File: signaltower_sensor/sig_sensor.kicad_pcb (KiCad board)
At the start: 2 copper layers, 44.6 x 39.3 mm, 6 parts, among them J1 5051100892_FFC-FPC_in, J2 5051100892_FFC-FPC_out, U1 BH1620FVC

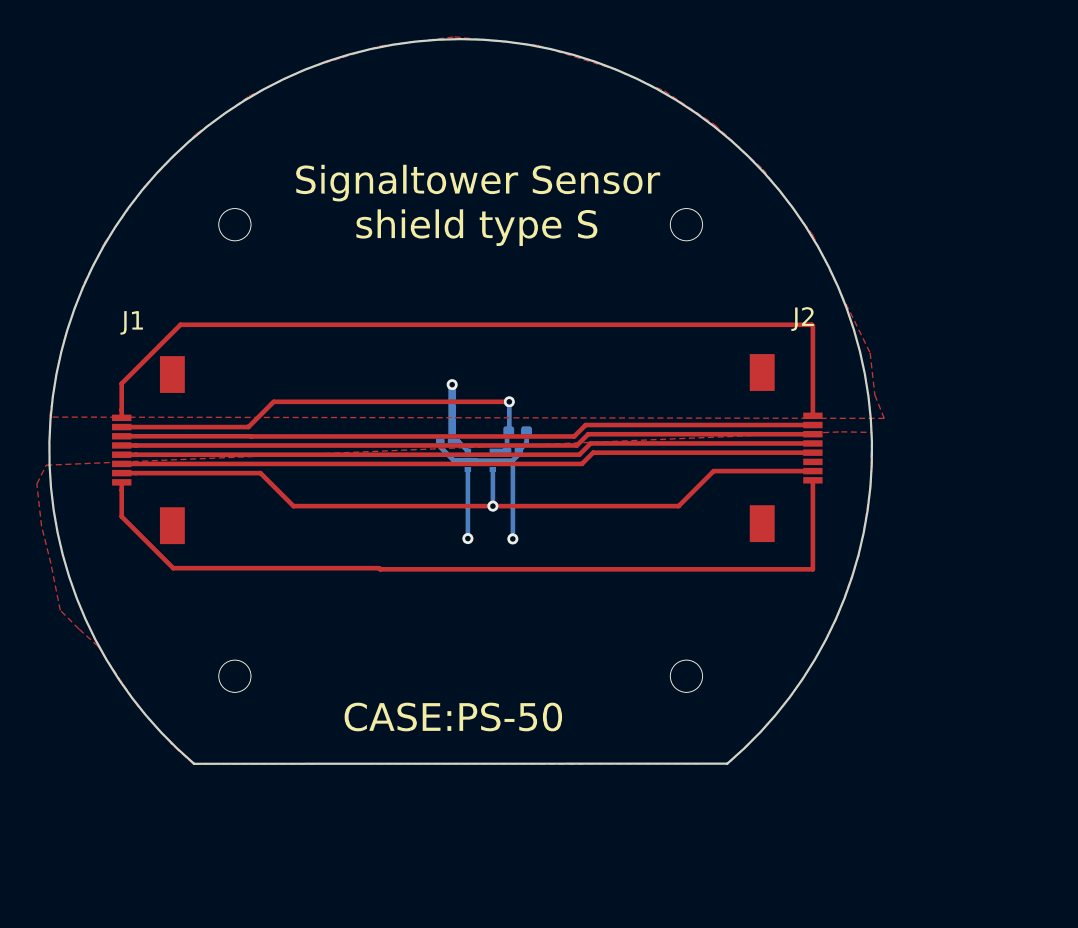
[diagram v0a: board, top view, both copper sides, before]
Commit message: update signal sensor host/slave
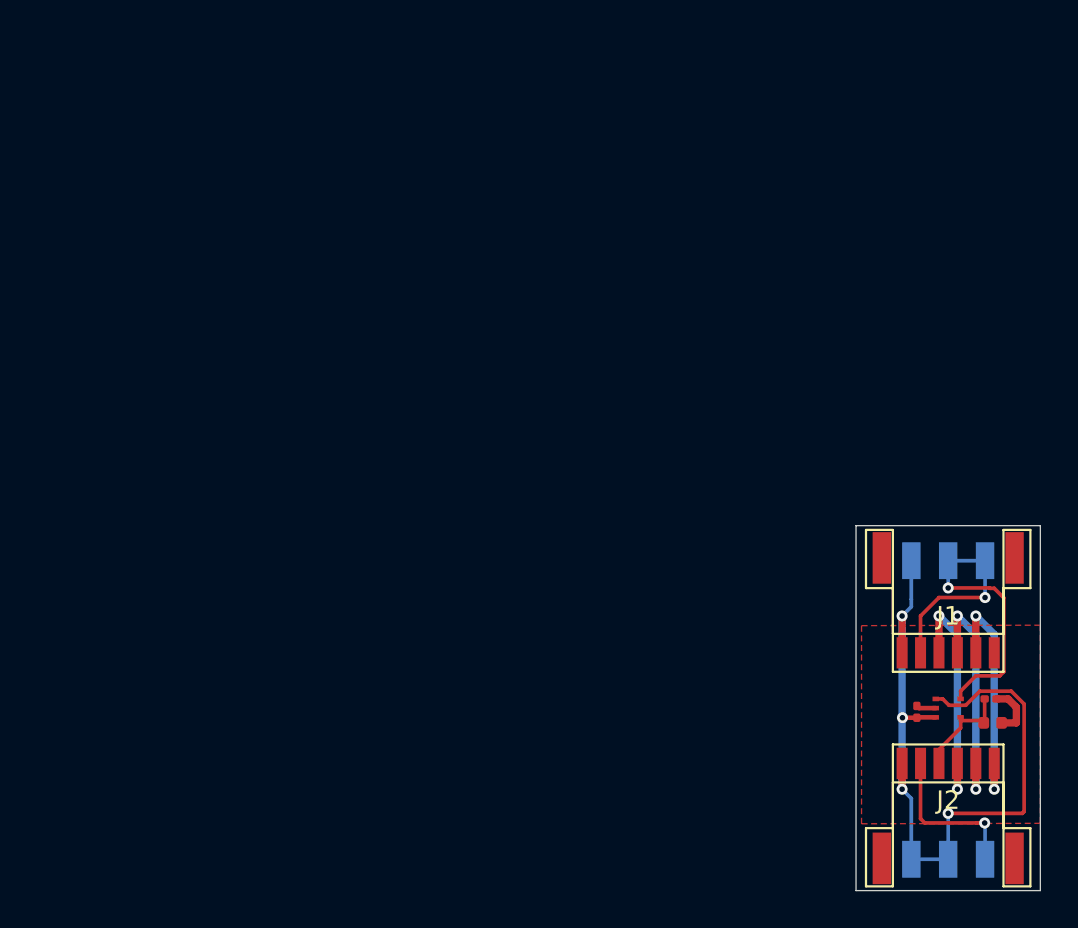
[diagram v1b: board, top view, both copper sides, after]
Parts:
- added SW1: SW_SPDT, lazurite_footprint:SHORT_SPDT, B.Cu at (180.0, 89.0)
- added SW2: SW_SPDT, lazurite_footprint:SHORT_SPDT, B.Cu at (180.0, 105.2)
- C1, C2, R1, U1: moved to F.Cu
- J1: value 5051100892_FFC-FPC_in -> Conn_01x06_Female; footprint lazurite_footprint:FFC-FPC_5051100892 -> Connector_JST:JST_NSH_SM06B_1mm_Horizonal
- J2: value 5051100892_FFC-FPC_out -> Conn_01x06_Female; footprint lazurite_footprint:FFC-FPC_5051100892 -> Connector_JST:JST_NSH_SM06B_1mm_Horizonal
- moved J1 45.7 mm to (180.0, 94.0), turned to 180 degrees
- moved R1 30.2 mm to (182.4, 97.8)
- moved C1 29.4 mm to (178.3, 97.2), turned to 90 degrees
- moved C2 29.2 mm to (182.3, 96.5)
- moved U1 28.7 mm to (180.5, 97.0), turned to 90 degrees
- moved J2 18.8 mm to (180.0, 100.0), turned to 0 degrees
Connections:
- C2 pad 1: /IOUT -> Net-(C2-Pad1)
- J1 pad 1: GND -> Net-(J1-Pad1)
- J1 pad 2: /GC2 -> /IOUT4
- J1 pad 3: /IOUT4 -> /IOUT2
- J1 pad 4: /IOUT3 -> /IOUT
- J1 pad 5: /IOUT2 -> GND
- J1 pad 6: /IOUT1 -> +3V3
- J2 pad 2: /IOUT1 -> GND
- J2 pad 3: /IOUT2 -> Net-(C2-Pad1)
- J2 pad 4: /IOUT3 -> /IOUT
- J2 pad 5: /IOUT4 -> /IOUT2
- J2 pad 6: Net-(J2-Pad6) -> /IOUT4
- R1 pad 1: /IOUT -> Net-(C2-Pad1)
- U1 pad 3: GND -> Net-(SW2-Pad2)
- U1 pad 4: /GC2 -> Net-(SW1-Pad2)
- U1 pad 5: /IOUT -> Net-(C2-Pad1)
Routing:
- net /GC2: track 41.0 -> 0.00 mm, vias 1 -> 0
- net GND: track 59.6 -> 20.6 mm
- net /IOUT1: track 37.8 -> 0.00 mm
- net /IOUT3: track 37.8 -> 0.00 mm
- net +3V3: track 49.7 -> 21.8 mm, vias 1 -> 3
- net /IOUT4: track 37.9 -> 13.2 mm, vias 0 -> 2
- net /IOUT2: track 37.8 -> 13.2 mm, vias 0 -> 2
- net Net-(SW2-Pad2): track 0.00 -> 18.0 mm, vias 0 -> 1
- net Net-(SW1-Pad2): track 0.00 -> 12.0 mm, vias 0 -> 1
- net /IOUT: track 25.1 -> 13.2 mm, vias 1 -> 2
- net Net-(C2-Pad1): track 0.00 -> 5.61 mm
- net (no net): vias 4 -> 0
- removed copper zone on F.Cu, net +3V3
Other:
- board size 44.6 x 39.3 mm -> 10 x 19.8 mm
- board text added: "HOST"
- board text added: "SLAVE"
- board text added: "Signal Tower Sensor"
- board text removed: "CASE:PS-50"
- board text removed: "Signaltower Sensor shield type S"

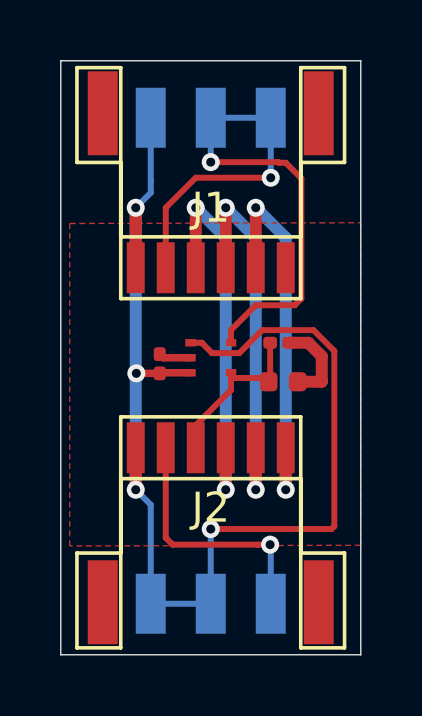
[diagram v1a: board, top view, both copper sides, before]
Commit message: signal tower sensor host/slave updated.
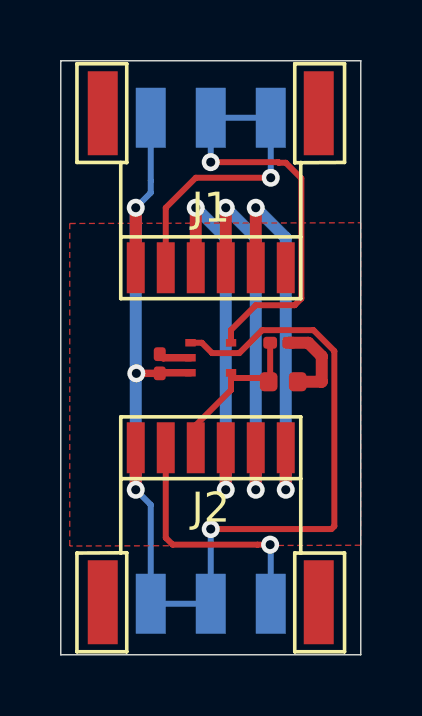
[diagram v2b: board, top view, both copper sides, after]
